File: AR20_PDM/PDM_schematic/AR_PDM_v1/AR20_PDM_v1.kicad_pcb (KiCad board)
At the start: 2 copper layers, 110 x 110 mm, 240 parts, among them J1 High_Curret_terminal, J2 1-776163-1, K1 DIPxx-1Cxx-51x, K2 DIPxx-1Cxx-51x, Q1 BTS50025-1TAD, Q10 N_FET, Q11 N_FET, Q12 N_FET, Q13 N_FET, Q14 N_FET, Q15 N_FET, Q16 N_FET, Q17 N_FET, Q2 BTS50025-1TAD, Q3 BTS50025-1TAD, Q4 BTS50025-1TAD, Q5 BTS50025-1TAD, Q6 BTS50025-1TAD, Q7 BTS50025-1TAD, Q8 N_FET, Q9 N_FET, SW1 SW_DIP_x07, SW2 SW_Push, U1 ACM_2020, U10 INA233, U11 INA233, U12 TCA6416A-PortExpander, U13 Fet-P, U14 Fet-P, U15 Fet-P, U16 Fet-P, U17 Fet-P, U18 Fet-P, U19 Fet-P, U2 INA233, U20 Fet-P, U21 Fet-P, U22 Fet-P, U23 Fet-P, U24 Fet-P, U25 Fet-P, U26 Fet-P, U27 Fet-P, U28 Fet-P, U29 Fet-P, U3 INA233, U30 Fet-P, U31 Fet-P, U4 INA233, U5 INA233, U6 INA233, U7 INA233, U8 INA233, U9 INA233

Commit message: PCB design, and misc, see description, work in progress
- added shutdown circuit for ACM shutdown capability
PCB layout, in progress: 
- added copper pour for 12 volt, for fuses
- arranged indicator LED's
- arranged some of the P1-P7 caps and resistors
- re arranged P1-p7 in ascending order.
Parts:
- moved R4 234.0 mm to (44.2, 126.0), turned to 270 degrees
- moved C7 225.4 mm to (46.0, 126.0), turned to 270 degrees
- moved U31 221.6 mm to (162.2, 46.1), turned to 180 degrees
- moved U28 220.3 mm to (178.2, 46.1), turned to 180 degrees
- moved R51 215.3 mm to (175.5, 46.1), turned to 270 degrees
- moved U30 212.3 mm to (156.8, 46.2), turned to 180 degrees
- moved R_in4 208.4 mm to (55.9, 126.0), turned to 270 degrees
- moved U29 203.6 mm to (172.8, 46.1), turned to 180 degrees
- moved U27 203.4 mm to (167.5, 46.1), turned to 180 degrees
- moved R56 198.0 mm to (164.8, 46.1), turned to 270 degrees
- moved C_in4 197.0 mm to (57.7, 126.0), turned to 270 degrees
- moved R54 184.1 mm to (159.5, 46.2), turned to 270 degrees
- moved C_in1 175.0 mm to (69.3, 126.0), turned to 270 degrees
- moved R_in1 169.2 mm to (67.6, 126.0), turned to 270 degrees
- moved R50 153.6 mm to (114.8, 40.9), turned to 270 degrees
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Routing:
- net vcc_5v: track 0.00 -> 54.0 mm, vias 0 -> 11
- net GND: track 171.7 -> 221.8 mm, vias 16 -> 34
- net V+12V: track 23.1 -> 50.7 mm
- net SDA: track 0.00 -> 21.3 mm, vias 0 -> 7
- net SLC: track 0.00 -> 18.4 mm, vias 0 -> 7
- net Net-(C_in3-Pad1): track 3.31 -> 20.1 mm, vias 1 -> 2
- net Net-(F1-Pad2): track 0.00 -> 13.7 mm
- net Net-(C_out1-Pad1): track 3.31 -> 14.8 mm
- net P2_OUT: track 0.00 -> 11.3 mm
- net P3_OUT: track 0.00 -> 11.3 mm
- net P7_OUT: track 0.00 -> 11.3 mm
- net P6_OUT: track 0.00 -> 11.3 mm
- net P5_OUT: track 0.00 -> 11.3 mm
- net P4_OUT: track 0.00 -> 11.3 mm
- net P1_OUT: track 0.00 -> 11.3 mm
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- added copper zone on F.Cu, net Net-(F1-Pad2)
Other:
- board size 110 x 110 mm -> 111.8 x 110 mm

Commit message: PCB Design, Work in progress
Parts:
- added D31: Shutdown_IN_Active, LED_SMD:LED_1206_3216Metric, F.Cu at (99.1, 53.8)
- added Q18: N_FET, Package_TO_SOT_SMD:SOT-23, B.Cu at (72.3, 135.4)
- added R59: 620R, Resistor_SMD:R_0603_1608Metric, F.Cu at (98.9, 49.9)
- added R_s13: 4K7, Resistor_SMD:R_0603_1608Metric, B.Cu at (72.4, 131.7)
- D23: value Shutdown_IN_Active -> Shutdown_Circuit_Active
- D5, D6, Q17, Q8, Q9, R1, R10, R11, R12, R14, R2, R20, R28, R3, R34, R37, R41, R43, R58, R7, R8, R9, U13, U15, U17, U19, U21, U23, U25: moved to B.Cu
- moved C6 257.0 mm to (34.8, 80.4)
- moved R5 251.1 mm to (34.7, 82.3)
- moved R_sense4 240.1 mm to (31.5, 80.5)
- moved C_sense4 239.1 mm to (31.4, 82.2)
- moved R3 229.3 mm to (49.0, 121.4), turned to 270 degrees
- moved C_sense1 224.2 mm to (27.8, 82.3)
- moved R_sense1 223.8 mm to (27.8, 80.6)
- moved C_sense5 211.6 mm to (24.4, 80.6)
- moved R_sense5 207.1 mm to (24.4, 82.3)
- moved R10 202.5 mm to (57.7, 122.5), turned to 270 degrees
- moved C_sense2 198.6 mm to (21.1, 80.6)
- moved R_sense2 197.4 mm to (21.1, 82.3)
- moved U18 186.7 mm to (143.3, 113.3), turned to 90 degrees
- moved U24 186.6 mm to (145.9, 126.0)
- moved U22 186.1 mm to (145.9, 122.4)
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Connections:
- net Net-(C8-Pad1) renamed /Phase1/P1_Shunt
- net Net-(C_out1-Pad1) renamed /Phase3/P3_Shunt
- net Net-(C_out2-Pad1) renamed /Phase5/P5_Shunt
- net Net-(C_out3-Pad1) renamed /Phase6_GearA/P6_Shunt
- net Net-(C_out4-Pad1) renamed /Phase2/P2_Shunt
- net Net-(C_out5-Pad1) renamed /Phase4/P4_Shunt
- net Net-(C_out6-Pad1) renamed /Phase7_GearB/P7_Shunt
- D10 pad 2: P2_OUT -> P2_Shunt
- D12 pad 2: P3_OUT -> P3_Shunt
- D14 pad 2: P4_OUT -> P4_Shunt
- D16 pad 2: P5_OUT -> P5_Shunt
- D18 pad 2: P6_OUT -> P6_Shunt
- D20 pad 2: P7_OUT -> P7_Shunt
- D23 pad 2: SHUTDOWN_IN -> Shutdown_Led
- D5 pad 1: SHUTDOWN_IN -> Shutdown_Led
- D6 pad 1: SHUTDOWN_IN -> Shutdown_Led
- D8 pad 2: P1_OUT -> P1_Shunt
- J2 pad 10: Net-(J2-Pad10) -> MCU_UNITS_FEED_OUT
- J2 pad 11: Net-(J2-Pad11) -> ETC_OUT
- J2 pad 12: Net-(J2-Pad12) -> CLUTCH_ACT_OUT
- J2 pad 13: Net-(J2-Pad13) -> COIL_INJECTOR_OUT
- J2 pad 14: Net-(J2-Pad14) -> SHUTDOWN_IN
- J2 pad 16: Net-(J2-Pad16) -> P2_EN_AUX
- J2 pad 17: Net-(J2-Pad17) -> P4_EN_AUX
- J2 pad 18: Net-(J2-Pad18) -> P6_EN_AUX
- J2 pad 19: Net-(J2-Pad19) -> P7_EN_AUX
- J2 pad 20: Net-(J2-Pad20) -> GND
- J2 pad 21: Net-(J2-Pad21) -> GND
- J2 pad 22: Net-(J2-Pad22) -> GND
- J2 pad 23: Net-(J2-Pad23) -> IGN_SWITCH_OUT
- J2 pad 24: Net-(J2-Pad24) -> FUEL_PUMP_OUT
- J2 pad 27: Net-(J2-Pad27) -> P1_EN_AUX
- J2 pad 28: Net-(J2-Pad28) -> P3_EN_AUX
- J2 pad 29: Net-(J2-Pad29) -> P5_EN_AUX
- J2 pad 35: Net-(J2-Pad35) -> SHUTDOWN_OUT
- J2 pad 9: Net-(J2-Pad9) -> GND
- K1 pad 6: SHUTDOWN_IN -> Shutdown_Led
- K2 pad 6: SHUTDOWN_IN -> Shutdown_Led
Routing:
- net GND: track 221.8 -> 474.5 mm, vias 34 -> 43
- net vcc_5v: track 54.0 -> 249.5 mm, vias 11 -> 12
- net SLC: track 18.4 -> 212.6 mm, vias 7 -> 12
- net SDA: track 21.3 -> 197.8 mm, vias 7 -> 10
- net Net-(K2-Pad14): track 0.00 -> 170.6 mm, vias 0 -> 7
- net Net-(K1-Pad14): track 0.00 -> 146.8 mm, vias 0 -> 4
- net P1_MOS_IN: track 7.20 -> 133.1 mm, vias 0 -> 2
- net FP_ENABLE_ACM: track 0.00 -> 113.1 mm
- net Shutdown_Led: track 0.00 -> 112.9 mm, vias 0 -> 1
- net FUEL_PUMP_OUT: track 0.00 -> 109.8 mm
- net P2_MOS_IN: track 7.20 -> 116.4 mm, vias 0 -> 2
- net COIL_INJECTOR_OUT: track 0.00 -> 105.1 mm
- net SHUTDOWN_IN: track 0.00 -> 100.5 mm
- net P3_MOS_IN: track 7.20 -> 105.2 mm, vias 0 -> 2
- net P4_MOS_IN: track 7.20 -> 97.7 mm, vias 0 -> 2
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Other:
- board size 111.8 x 110 mm -> 110 x 110 mm
- board text added: "Remember to double check, relay coil activation polarity"

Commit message: PCB Design,  minor schematics changes, work in progress, see description
- Removed mos sense caps and resistors accept one, 
since only one measurement can be done, at a time.
- added mos sens protection resistors on each line, to protect mux mosfets and micro controller. 
- Routing plan mostly finalized, some of the traces are just proof of concept.
those needs to be routed nicely.
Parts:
- removed C6, C_sense2, C_sense3, C_sense4, C_sense5, C_sense6: 10nf, Capacitor_SMD:C_0603_1608Metric
- added R_sense1: 1k, Resistor_SMD:R_0603_1608Metric, F.Cu at (97.2, 68.2)
- Q10, Q11, Q12, Q13, Q14, Q15, Q16, R_s10, R_s11, R_s12, R_s6, R_s7, R_s8, R_s9: moved to B.Cu
- R5, R_sense2, R_sense3, R_sense4, R_sense6: value 1k -> 4k7
- moved Q10 160.2 mm to (52.6, 105.8), turned to 270 degrees
- moved Q11 153.0 mm to (64.3, 105.8), turned to 270 degrees
- moved R_s7 140.1 mm to (64.3, 103.3)
- moved Q12 136.7 mm to (75.9, 105.8), turned to 270 degrees
- moved R_s8 134.1 mm to (75.9, 103.3)
- moved Q13 129.4 mm to (87.6, 105.8), turned to 270 degrees
- moved Q14 122.5 mm to (99.3, 105.8), turned to 270 degrees
- moved R_s9 120.8 mm to (87.6, 103.3)
- moved R_s10 114.8 mm to (99.3, 103.3)
- moved R_s11 107.1 mm to (111.0, 103.3)
- moved R_s12 99.5 mm to (122.7, 103.3)
- moved Q16 98.9 mm to (122.7, 105.8), turned to 270 degrees
- moved Q15 97.2 mm to (111.0, 105.8), turned to 270 degrees
- moved C_sense1 70.5 mm to (97.2, 69.7), turned to 180 degrees
- moved R5 55.5 mm to (-2.79, 41.4)
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- renumbered R_sense1 to 4k7
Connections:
- 4k7 pad 1: P3_MOS_SENSE -> Net-(4k7-Pad1)
- 4k7 pad 2: GND -> P3_MOS_SENSE
- C8 pad 1: /Phase1/P1_Shunt -> P1_Shunt
- C_out1 pad 1: /Phase3/P3_Shunt -> P3_Shunt
- C_out2 pad 1: /Phase5/P5_Shunt -> P5_Shunt
- C_out3 pad 1: /Phase6_GearA/P6_Shunt -> P6_Shunt
- C_out4 pad 1: /Phase2/P2_Shunt -> P2_Shunt
- C_out5 pad 1: /Phase4/P4_Shunt -> P4_Shunt
- C_out6 pad 1: /Phase7_GearB/P7_Shunt -> P7_Shunt
- C_sense1 pad 2: P3_MOS_SENSE -> MOS_SENSE_ALL
- Q1 pad 3: P1_MOS_SENSE -> Net-(Q1-Pad3)
- Q1 pad 5: /Phase1/P1_Shunt -> P1_Shunt
- Q1 pad 6: /Phase1/P1_Shunt -> P1_Shunt
- Q1 pad 7: /Phase1/P1_Shunt -> P1_Shunt
- Q2 pad 3: P2_MOS_SENSE -> Net-(Q2-Pad3)
- Q2 pad 5: /Phase2/P2_Shunt -> P2_Shunt
- Q2 pad 6: /Phase2/P2_Shunt -> P2_Shunt
- Q2 pad 7: /Phase2/P2_Shunt -> P2_Shunt
- Q3 pad 3: P3_MOS_SENSE -> Net-(4k7-Pad1)
- Q3 pad 5: /Phase3/P3_Shunt -> P3_Shunt
- Q3 pad 6: /Phase3/P3_Shunt -> P3_Shunt
- Q3 pad 7: /Phase3/P3_Shunt -> P3_Shunt
- Q4 pad 3: P4_MOS_SENSE -> Net-(Q4-Pad3)
- Q4 pad 5: /Phase4/P4_Shunt -> P4_Shunt
- Q4 pad 6: /Phase4/P4_Shunt -> P4_Shunt
- Q4 pad 7: /Phase4/P4_Shunt -> P4_Shunt
- Q5 pad 3: P5_MOS_SENSE -> Net-(Q5-Pad3)
- Q5 pad 5: /Phase5/P5_Shunt -> P5_Shunt
- Q5 pad 6: /Phase5/P5_Shunt -> P5_Shunt
- Q5 pad 7: /Phase5/P5_Shunt -> P5_Shunt
- Q6 pad 3: P6_MOS_SENSE -> Net-(Q6-Pad3)
- Q6 pad 5: /Phase6_GearA/P6_Shunt -> P6_Shunt
- Q6 pad 6: /Phase6_GearA/P6_Shunt -> P6_Shunt
- Q6 pad 7: /Phase6_GearA/P6_Shunt -> P6_Shunt
- Q7 pad 3: P7_MOS_SENSE -> Net-(Q7-Pad3)
- Q7 pad 5: /Phase7_GearB/P7_Shunt -> P7_Shunt
- Q7 pad 6: /Phase7_GearB/P7_Shunt -> P7_Shunt
- Q7 pad 7: /Phase7_GearB/P7_Shunt -> P7_Shunt
- R5 pad 1: P1_MOS_SENSE -> Net-(Q1-Pad3)
- R5 pad 2: GND -> P1_MOS_SENSE
- R_Shunt10 pad 2: /Phase7_GearB/P7_Shunt -> P7_Shunt
- R_Shunt4 pad 2: /Phase1/P1_Shunt -> P1_Shunt
- R_Shunt5 pad 2: /Phase3/P3_Shunt -> P3_Shunt
- R_Shunt6 pad 2: /Phase5/P5_Shunt -> P5_Shunt
- R_Shunt7 pad 2: /Phase6_GearA/P6_Shunt -> P6_Shunt
- R_Shunt8 pad 2: /Phase2/P2_Shunt -> P2_Shunt
- R_Shunt9 pad 2: /Phase4/P4_Shunt -> P4_Shunt
- R_sense2 pad 1: P5_MOS_SENSE -> Net-(Q5-Pad3)
- R_sense2 pad 2: GND -> P5_MOS_SENSE
- R_sense3 pad 1: P6_MOS_SENSE -> Net-(Q6-Pad3)
- R_sense3 pad 2: GND -> P6_MOS_SENSE
- R_sense4 pad 1: P2_MOS_SENSE -> Net-(Q2-Pad3)
- R_sense4 pad 2: GND -> P2_MOS_SENSE
- R_sense5 pad 1: P4_MOS_SENSE -> Net-(Q4-Pad3)
- R_sense5 pad 2: GND -> P4_MOS_SENSE
- R_sense6 pad 1: P7_MOS_SENSE -> Net-(Q7-Pad3)
- R_sense6 pad 2: GND -> P7_MOS_SENSE
- U10 pad 8: /Phase4/P4_Shunt -> P4_Shunt
- U10 pad 9: /Phase4/P4_Shunt -> P4_Shunt
- U11 pad 8: /Phase7_GearB/P7_Shunt -> P7_Shunt
- U11 pad 9: /Phase7_GearB/P7_Shunt -> P7_Shunt
- U5 pad 8: /Phase1/P1_Shunt -> P1_Shunt
- U5 pad 9: /Phase1/P1_Shunt -> P1_Shunt
- U6 pad 8: /Phase3/P3_Shunt -> P3_Shunt
- U6 pad 9: /Phase3/P3_Shunt -> P3_Shunt
- U7 pad 8: /Phase5/P5_Shunt -> P5_Shunt
- U7 pad 9: /Phase5/P5_Shunt -> P5_Shunt
- U8 pad 8: /Phase6_GearA/P6_Shunt -> P6_Shunt
- U8 pad 9: /Phase6_GearA/P6_Shunt -> P6_Shunt
- U9 pad 8: /Phase2/P2_Shunt -> P2_Shunt
- U9 pad 9: /Phase2/P2_Shunt -> P2_Shunt
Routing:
- net MOS_SENSE_ALL: track 0.00 -> 232.6 mm, vias 0 -> 8
- net GND: track 474.5 -> 582.4 mm
- net P7_Shunt: track 0.00 -> 72.8 mm, vias 0 -> 2
- net (no net): track 0.00 -> 72.1 mm
- net ACM_Shutdown_Circuit: track 72.9 -> 141.4 mm
- net P6_Shunt: track 0.00 -> 61.6 mm, vias 0 -> 2
- net P1_MOS_SENSE_Select: track 0.00 -> 59.6 mm, vias 0 -> 1
- net P1_Shunt: track 0.00 -> 54.9 mm, vias 0 -> 2
- net P5_Shunt: track 0.00 -> 51.8 mm, vias 0 -> 2
- net P2_Shunt: track 0.00 -> 51.7 mm, vias 0 -> 2
- net P2_MOS_SENSE_Select: track 0.00 -> 49.0 mm, vias 0 -> 1
- net P7_MOS_SENSE_Select: track 0.00 -> 48.4 mm, vias 0 -> 1
- net P4_Shunt: track 0.00 -> 47.0 mm, vias 0 -> 2
- net P3_Shunt: track 0.00 -> 44.6 mm, vias 0 -> 2
- net P3_MOS_SENSE_Select: track 0.00 -> 38.9 mm, vias 0 -> 1
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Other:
- board text added: "WORK IN PROGRESS :)"
- board text added: "protection resistor, mos sens Tenkte å plasere desse ved main mosfeten, på undersia, attmed de små mux mosfettene"

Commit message: First Complete Draft of PCB and schematics, - minus see discription
- missing correct smd switch header
- missing correct main power plug
- tweeks still needs to be done
- Extra inspection of schematics pending
- proper, in depth quiality controll of pcb work pending
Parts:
- 4k7, R16, R18, R22, R24, R26, R30, R32, R5, R_sense2, R_sense3, R_sense4, R_sense5, R_sense6: moved to B.Cu
- U12: value TCA6416A-PortExpander -> TCA6424ARGJR; footprint AR_PDM_v1:SOP65P640X120-24N -> AR_PDM_v1:QFN50P500X500X60-33N
- moved SW2 207.0 mm to (145.8, 90.6), turned to 90 degrees
- moved R53 191.3 mm to (141.5, 93.5), turned to 180 degrees
- moved R_sense6 159.6 mm to (122.1, 108.3)
- moved R_sense3 146.1 mm to (111.0, 107.1), turned to 180 degrees
- moved R_sense2 133.0 mm to (99.3, 107.1), turned to 180 degrees
- moved R_sense5 120.1 mm to (87.6, 107.1), turned to 180 degrees
- moved 4k7 108.0 mm to (75.9, 107.1), turned to 180 degrees
- moved R10K1 104.1 mm to (97.2, 78.7), turned to 180 degrees
- moved R10K2 103.7 mm to (97.2, 77.1), turned to 180 degrees
- moved R_sense4 96.2 mm to (64.3, 107.1), turned to 180 degrees
- moved R5 85.9 mm to (52.6, 107.1), turned to 180 degrees
- moved J1 55.8 mm to (48.8, 92.1)
- moved R49 37.1 mm to (138.2, 70.2), turned to 90 degrees
- moved U28 34.3 mm to (140.8, 70.2), turned to 0 degrees
- moved R51 31.1 mm to (138.2, 66.5), turned to 90 degrees
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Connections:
- net DIRECT_Alert renamed /Fuses_Direct/DIRECT_Alert
- J2 pad 1: Net-(J2-Pad1) -> P1_OUT
- J2 pad 14: SHUTDOWN_IN -> P6_GearA_open_drain_output
- J2 pad 15: Net-(J2-Pad15) -> TX
- J2 pad 2: Net-(J2-Pad2) -> P2_OUT
- J2 pad 25: Net-(J2-Pad25) -> SHUTDOWN_IN
- J2 pad 26: Net-(J2-Pad26) -> RX
- J2 pad 3: Net-(J2-Pad3) -> FP_ENABLE_AUX
- J2 pad 30: Net-(J2-Pad30) -> FP_ENABLE_RELAY_SINK
- J2 pad 33: Net-(J2-Pad33) -> CAN_LOW
- J2 pad 34: Net-(J2-Pad34) -> CAN_HIGH
- J2 pad 4: Net-(J2-Pad4) -> P3_OUT
- J2 pad 5: Net-(J2-Pad5) -> P4_OUT
- J2 pad 6: Net-(J2-Pad6) -> P5_OUT
- J2 pad 7: Net-(J2-Pad7) -> P6_OUT
- J2 pad 8: Net-(J2-Pad8) -> P7_OUT
- Pullup1 pad 1: vcc_5v -> Net-(Pullup1-Pad1)
- Pullup1 pad 2: Net-(Pullup1-Pad2) -> vcc_5v
- Q1 pad 4: V+12V -> Net-(Q1-Pad4)
- Q11 pad 3: P4_MOS_SENSE -> P2_MOS_SENSE
- Q13 pad 3: P2_MOS_SENSE -> P4_MOS_SENSE
- Q2 pad 4: V+12V -> Net-(Q2-Pad4)
- Q3 pad 4: V+12V -> Net-(Q3-Pad4)
- Q4 pad 4: V+12V -> Net-(Q4-Pad4)
- Q5 pad 4: V+12V -> Net-(Q5-Pad4)
- Q6 pad 4: V+12V -> Net-(Q6-Pad4)
- Q7 pad 4: V+12V -> Net-(Q7-Pad4)
- U1 pad 1: MOS_SENSE_ALL -> ACM_Shutdown_Circuit
- U1 pad 19: GND -> Net-(U1-Pad19)
- U1 pad 20: P1_EN_ACM -> Switch
- U1 pad 21: GND -> Net-(U1-Pad21)
- U1 pad 22: FP_ENABLE_ACM -> P1_EN_ACM
- U1 pad 5: Net-(U1-Pad5) -> MOS_SENSE_ALL
- U1 pad 9: GND -> Net-(U1-Pad9)
- U12 pad 1: Net-(Pullup2-Pad2) -> P1_Fault
- U12 pad 10: P6_Fault -> P1_MOS_SENSE_Select
- U12 pad 11: P7_Fault -> P2_MOS_SENSE_Select
- U12 pad 12: GND -> P3_MOS_SENSE_Select
- U12 pad 13: FUEL_PUMP_Fault -> P4_MOS_SENSE_Select
- U12 pad 14: P1_MOS_SENSE_Select -> P5_MOS_SENSE_Select
- U12 pad 15: P2_MOS_SENSE_Select -> P6_MOS_SENSE_Select
- U12 pad 16: P3_MOS_SENSE_Select -> P7_MOS_SENSE_Select
- U12 pad 17: P4_MOS_SENSE_Select -> FP_Alert
- U12 pad 18: P5_MOS_SENSE_Select -> COIL_INJECTOR_Alert
- U12 pad 19: P6_MOS_SENSE_Select -> Net-(U12-Pad19)
- U12 pad 2: vcc_5v -> P2_Fault
- U12 pad 20: P7_MOS_SENSE_Select -> FP_ENABLE_ACM
- U12 pad 21: GND -> Net-(U12-Pad21)
- U12 pad 22: SLC -> Net-(U12-Pad22)
- U12 pad 23: SDA -> Net-(U12-Pad23)
- U12 pad 24: vcc_5v -> Net-(U12-Pad24)
- U12 pad 3: Net-(Pullup1-Pad2) -> P3_Fault
- U12 pad 4: COIL_INJECTOR_Fault -> P4_Fault
- U12 pad 5: P1_Fault -> P5_Fault
- U12 pad 6: P2_Fault -> P6_Fault
- U12 pad 7: P3_Fault -> P7_Fault
- U12 pad 8: P4_Fault -> COIL_INJECTOR_Fault
- U12 pad 9: P5_Fault -> FUEL_PUMP_Fault
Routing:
- net GND: track 582.4 -> 1070.0 mm, vias 43 -> 55
- net vcc_5v: track 256.2 -> 554.6 mm, vias 12 -> 19
- net SLC: track 212.6 -> 413.2 mm, vias 12 -> 17
- net SDA: track 197.8 -> 395.2 mm, vias 10 -> 15
- net RX: track 0.00 -> 177.8 mm, vias 0 -> 2
- net TX: track 0.00 -> 175.4 mm, vias 0 -> 2
- net Switch: track 0.00 -> 140.0 mm, vias 0 -> 2
- net CAN_LOW: track 0.00 -> 111.6 mm, vias 0 -> 2
- net CAN_HIGH: track 0.00 -> 111.0 mm, vias 0 -> 2
- net COIL_INJECTOR_OUT: track 105.1 -> 212.5 mm, vias 0 -> 1
- net FUEL_PUMP_OUT: track 109.8 -> 217.2 mm, vias 0 -> 1
- net Shutdown_Led: track 112.9 -> 217.2 mm, vias 1 -> 2
- net SHUTDOWN_IN: track 100.5 -> 204.7 mm, vias 0 -> 1
- net P6_MOS_IN: track 72.0 -> 158.2 mm, vias 2 -> 4
- net COIL_INJECTOR_Fault: track 0.00 -> 73.2 mm, vias 0 -> 2
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- added copper zone on B.Cu, net GND
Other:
- board text removed: "Remember to double check, relay coil activation polarity"
- board text removed: "WORK IN PROGRESS :)"
- board text removed: "protection resistor, mos sens Tenkte å plasere desse ved main mosfeten, på undersia, attmed de små mux mosfettene"

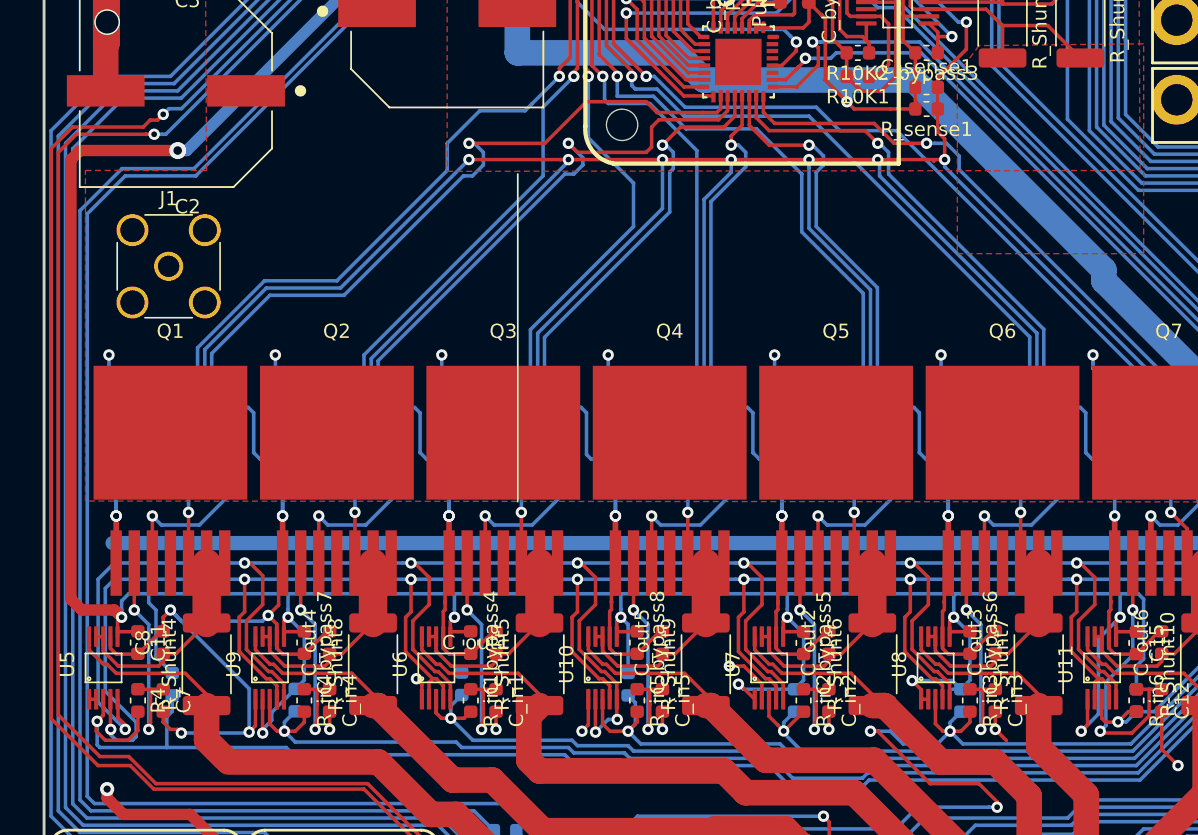
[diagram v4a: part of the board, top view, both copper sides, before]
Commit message: DRC, work Fixed couple of unconnected items
- Main power connection is still missing
- Button connector still missing
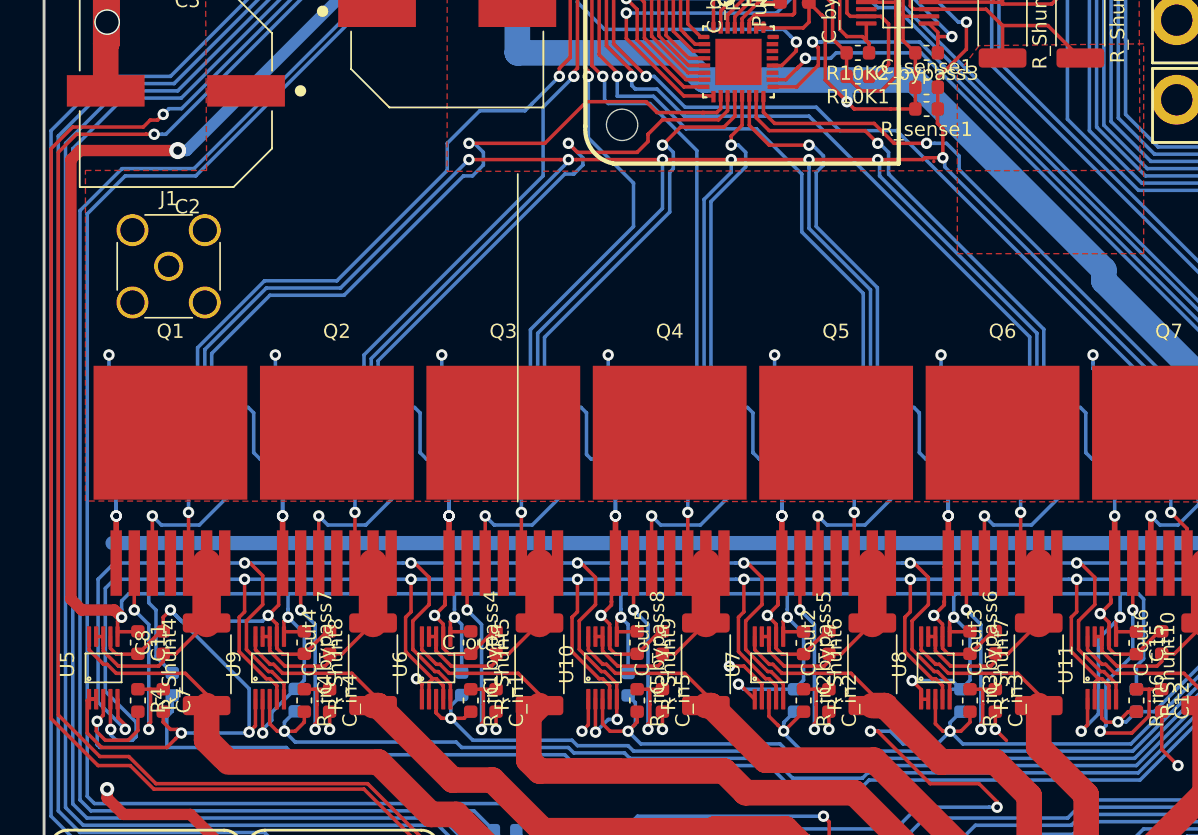
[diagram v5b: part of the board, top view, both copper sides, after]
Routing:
- net GND: track 1070.0 -> 1083.0 mm, vias 55 -> 60
- net vcc_5v: track 554.6 -> 558.7 mm
- net P2_MOS_SENSE_Select: track 42.1 -> 41.6 mm
